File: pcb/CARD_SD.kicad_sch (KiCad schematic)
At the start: 12 parts, among them J8 MEM2052-00-195-00-A

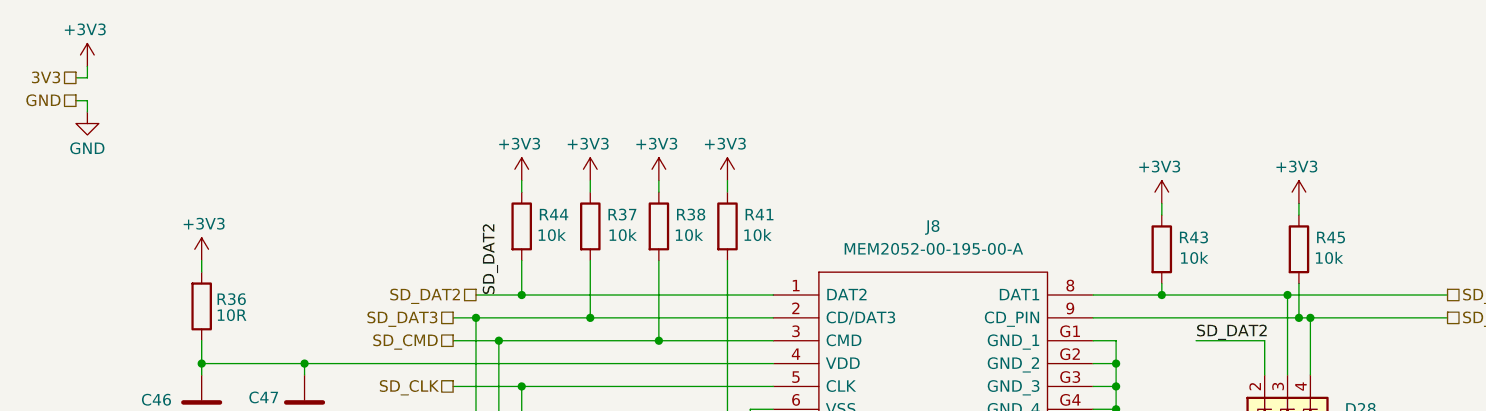
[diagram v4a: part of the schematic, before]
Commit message: removed AGND and added ground garden
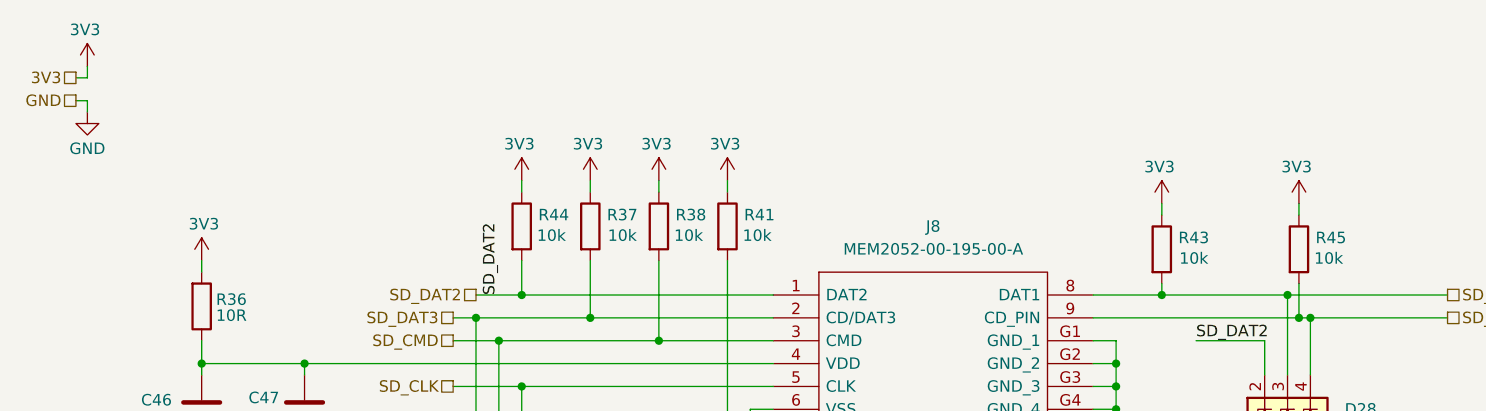
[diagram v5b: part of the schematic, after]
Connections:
- net +3V3 renamed 3V3
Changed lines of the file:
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@@
 			)
 		)
-		(property "Value" "+3V3"
+		(property "Value" "3V3"
 			(at 89.916 32.766 0)
 			(effects
@@
 			)
 		)
-		(property "Value" "+3V3"
+		(property "Value" "3V3"
 			(at 74.676 32.766 0)
 			(effects
@@
 			)
 		)
-		(property "Value" "+3V3"
+		(property "Value" "3V3"
 			(at 145.796 35.306 0)
 			(effects
@@
 			)
 		)
-		(property "Value" "+3V3"
+		(property "Value" "3V3"
 			(at 26.416 20.066 0)
 			(effects
@@
 			)
 		)
-		(property "Value" "+3V3"
+		(property "Value" "3V3"
 			(at 82.296 32.766 0)
 			(effects
@@
 			)
 		)
-		(property "Value" "+3V3"
+		(property "Value" "3V3"
 			(at 97.536 32.766 0)
 			(effects
@@
 			)
 		)
-		(property "Value" "+3V3"
+		(property "Value" "3V3"
 			(at 161.036 35.306 0)
 			(effects
@@
 			)
 		)
-		(property "Value" "+3V3"
+		(property "Value" "3V3"
 			(at 39.624 41.656 0)
 			(effects

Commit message: updates from bom release
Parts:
- C46: value 10uF -> 10u
- C47: value 100nF -> 100n
- R36: value 10R -> 10
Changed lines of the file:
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@@
 			)
 		)
-		(property "Value" "10R"
+		(property "Value" "10"
 			(at 42.672 51.816 0)
 			(effects
@@
 			)
 		)
-		(property "Value" "10uF"
+		(property "Value" "10u"
 			(at 36.068 63.5 0)
 			(effects
@@
 			)
 		)
-		(property "Value" "100nF"
+		(property "Value" "100n"
 			(at 48.006 63.5 0)
 			(effects
